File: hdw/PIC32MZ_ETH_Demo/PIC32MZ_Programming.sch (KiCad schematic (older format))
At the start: 10 parts

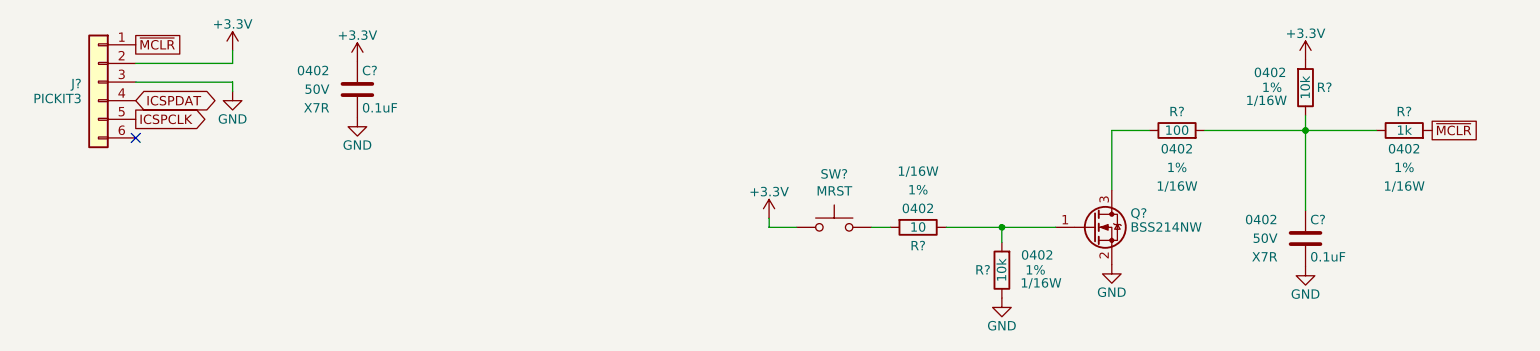
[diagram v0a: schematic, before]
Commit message: More schematic tweaks, followed PHY design guide
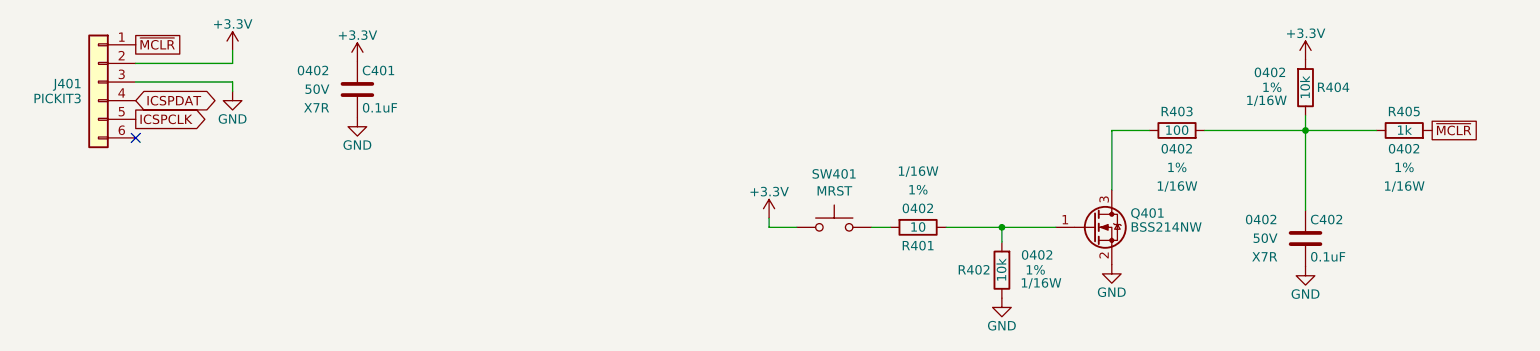
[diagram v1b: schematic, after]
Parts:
- gave numbers to parts that had none: 10
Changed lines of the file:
@@
 EESchema Schematic File Version 4
+LIBS:PIC32MZ_ETH_Demo-cache
 EELAYER 30 0
 EELAYER END
@@
 $EndDescr
 $Comp
-L Connector_Generic:Conn_01x06 J?
+L Connector_Generic:Conn_01x06 J401
 U 1 1 5BB4A695
 P 1070 1990
-F 0 "J?" H 1160 1980 50  0000 L CNN
+F 0 "J401" H 1160 1980 50  0000 L CNN
 F 1 "PICKIT3" H 1160 1900 50  0000 L CNN
 F 2 "Custom Footprints Library:PICKIT3_Header" H 1070 1990 50  0001 C CNN
@@
 ICSPCLK
 $Comp
-L power:GND #PWR?
+L power:GND #PWR0402
 U 1 1 5BB4A7C4
 P 1790 2040
-F 0 "#PWR?" H 1790 1790 50  0001 C CNN
+F 0 "#PWR0402" H 1790 1790 50  0001 C CNN
 F 1 "GND" H 1790 1890 50  0000 C CNN
 F 2 "" H 1790 2040 50  0001 C CNN
@@
 NoConn ~ 1270 2290
 $Comp
-L Custom_Library:C_Custom C?
+L Custom_Library:C_Custom C401
 U 1 1 5BC13497
 P 2460 2030
-F 0 "C?" H 2485 2130 50  0000 L CNN
+F 0 "C401" H 2485 2130 50  0000 L CNN
 F 1 "0.1uF" H 2485 1930 50  0000 L CNN
 F 2 "Capacitors_SMD:C_0402" H 2498 1880 50  0001 C CNN
@@
 $EndComp
 $Comp
-L power:GND #PWR?
+L power:GND #PWR0404
 U 1 1 5BC1349E
 P 2460 2180
-F 0 "#PWR?" H 2460 1930 50  0001 C CNN
+F 0 "#PWR0404" H 2460 1930 50  0001 C CNN
 F 1 "GND" H 2460 2030 50  0000 C CNN
 F 2 "" H 2460 2180 50  0001 C CNN
@@
 AR Path="/5C1D5CB6/5BC152E5" Ref="R?"  Part="1"
 AR Path="/5CB0BC26/5BC152E5" Ref="R?"  Part="1"
-AR Path="/5E697920/5BC152E5" Ref="R?"  Part="1"
-F 0 "R?" H 7490 2020 50  0000 R CNN
+AR Path="/5E697920/5BC152E5" Ref="R404"  Part="1"
+F 0 "R404" H 7490 2020 50  0000 R CNN
 F 1 "10k" V 7550 2020 50  0000 C CNN
 F 2 "Resistors_SMD:R_0402" H 7550 2020 50  0001 C CNN
@@
 $EndComp
 $Comp
-L Custom_Library:C_Custom C?
+L Custom_Library:C_Custom C402
 U 1 1 5BC1574E
 P 7550 2830
-F 0 "C?" H 7575 2930 50  0000 L CNN
+F 0 "C402" H 7575 2930 50  0000 L CNN
 F 1 "0.1uF" H 7575 2730 50  0000 L CNN
 F 2 "Capacitors_SMD:C_0402" H 7588 2680 50  0001 C CNN
@@
 $EndComp
 $Comp
-L power:GND #PWR?
+L power:GND #PWR0409
 U 1 1 5BC15E18
 P 7550 2980
-F 0 "#PWR?" H 7550 2730 50  0001 C CNN
+F 0 "#PWR0409" H 7550 2730 50  0001 C CNN
 F 1 "GND" H 7550 2830 50  0000 C CNN
 F 2 "" H 7550 2980 50  0001 C CNN
@@
 $EndComp
 $Comp
-L Custom_Library:R_Custom R?
+L Custom_Library:R_Custom R405
 U 1 1 5BC16316
 P 8080 2250
-F 0 "R?" V 7980 2250 50  0000 C CNN
+F 0 "R405" V 7980 2250 50  0000 C CNN
 F 1 "1k" V 8080 2250 50  0000 C CNN
 F 2 "Resistors_SMD:R_0402" H 8080 2250 50  0001 C CNN
@@
 ~MCLR
 $Comp
-L Switch:SW_Push SW?
+L Switch:SW_Push SW401
 U 1 1 5BC17B44
 P 5020 2770
-F 0 "SW?" H 5020 3055 50  0000 C CNN
+F 0 "SW401" H 5020 3055 50  0000 C CNN
 F 1 "MRST" H 5020 2964 50  0000 C CNN
 F 2 "Buttons_Switches_THT:SW_PUSH_6mm" H 5020 2970 50  0001 C CNN
@@
 $EndComp
 $Comp
-L Custom_Library:R_Custom R?
+L Custom_Library:R_Custom R403
 U 1 1 5BC190FF
 P 6860 2250
-F 0 "R?" V 6760 2250 50  0000 C CNN
+F 0 "R403" V 6760 2250 50  0000 C CNN
 F 1 "100" V 6860 2250 50  0000 C CNN
 F 2 "Resistors_SMD:R_0402" H 6860 2250 50  0001 C CNN
@@
 	7010 2250 7550 2250
 $Comp
-L power:GND #PWR?
+L power:GND #PWR0407
 U 1 1 5BE087C1
 P 6510 2970
-F 0 "#PWR?" H 6510 2720 50  0001 C CNN
+F 0 "#PWR0407" H 6510 2720 50  0001 C CNN
 F 1 "GND" H 6510 2820 50  0000 C CNN
 F 2 "" H 6510 2970 50  0001 C CNN
@@
 $EndComp
 $Comp
-L Custom_Library:R_Custom R?
+L Custom_Library:R_Custom R401
 U 1 1 5BE087CB
 P 5470 2770
-F 0 "R?" V 5370 2770 50  0000 C CNN
+F 0 "R401" V 5370 2770 50  0000 C CNN
 F 1 "10" V 5470 2770 50  0000 C CNN
 F 2 "Resistors_SMD:R_0402" H 5470 2770 50  0001 C CNN
@@
 AR Path="/5C1D5CB6/5BE087D6" Ref="R?"  Part="1"
 AR Path="/5CB0BC26/5BE087D6" Ref="R?"  Part="1"
-AR Path="/5E697920/5BE087D6" Ref="R?"  Part="1"
-F 0 "R?" H 5860 3000 50  0000 R CNN
+AR Path="/5E697920/5BE087D6" Ref="R402"  Part="1"
+F 0 "R402" H 5860 3000 50  0000 R CNN
 F 1 "10k" V 5920 3000 50  0000 C CNN
 F 2 "Resistors_SMD:R_0402" H 5920 3000 50  0001 C CNN
@@
 $EndComp
 $Comp
-L power:GND #PWR?
+L power:GND #PWR0406
 U 1 1 5BE087DD
 P 5920 3150
-F 0 "#PWR?" H 5920 2900 50  0001 C CNN
+F 0 "#PWR0406" H 5920 2900 50  0001 C CNN
 F 1 "GND" H 5920 3000 50  0000 C CNN
 F 2 "" H 5920 3150 50  0001 C CNN
@@
 	7550 2680 7550 2250
 $Comp
-L power:+3.3V #PWR?
+L power:+3.3V #PWR0405
 U 1 1 5E6EB62A
 P 4670 2720
-F 0 "#PWR?" H 4670 2570 50  0001 C CNN
+F 0 "#PWR0405" H 4670 2570 50  0001 C CNN
 F 1 "+3.3V" H 4670 2860 50  0000 C CNN
 F 2 "" H 4670 2720 50  0001 C CNN
@@
 $EndComp
 $Comp
-L power:+3.3V #PWR?
+L power:+3.3V #PWR0408
 U 1 1 5E6EBFA5
 P 7550 1870
-F 0 "#PWR?" H 7550 1720 50  0001 C CNN
+F 0 "#PWR0408" H 7550 1720 50  0001 C CNN
 F 1 "+3.3V" H 7550 2010 50  0000 C CNN
 F 2 "" H 7550 1870 50  0001 C CNN
@@
 $EndComp
 $Comp
-L power:+3.3V #PWR?
+L power:+3.3V #PWR0403
 U 1 1 5E6EC62F
 P 2460 1880
-F 0 "#PWR?" H 2460 1730 50  0001 C CNN
+F 0 "#PWR0403" H 2460 1730 50  0001 C CNN
 F 1 "+3.3V" H 2460 2020 50  0000 C CNN
 F 2 "" H 2460 1880 50  0001 C CNN
@@
 $EndComp
 $Comp
-L power:+3.3V #PWR?
+L power:+3.3V #PWR0401
 U 1 1 5E6ECA36
 P 1790 1820
-F 0 "#PWR?" H 1790 1670 50  0001 C CNN
+F 0 "#PWR0401" H 1790 1670 50  0001 C CNN
 F 1 "+3.3V" H 1790 1960 50  0000 C CNN
 F 2 "" H 1790 1820 50  0001 C CNN
@@
 $EndComp
 $Comp
-L Transistor_FET:BSS214NW Q?
+L Transistor_FET:BSS214NW Q401
 U 1 1 5E765004
 P 6410 2770
-F 0 "Q?" H 6610 2845 50  0000 L CNN
+F 0 "Q401" H 6610 2845 50  0000 L CNN
 F 1 "BSS214NW" H 6610 2770 50  0000 L CNN
 F 2 "Package_TO_SOT_SMD:SOT-323_SC-70" H 6610 2695 50  0001 L CIN

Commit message: Populated digi-key pn's
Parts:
- C401, C402: Digi-Key PN (none) -> 490-10701-1-ND
- R401: Digi-Key PN (none) -> 541-3964-1-ND
- R402, R404: Digi-Key PN (none) -> RMCF0402FT10K0CT-ND
- R403: Digi-Key PN (none) -> 541-100LCT-ND
- R405: Digi-Key PN (none) -> 541-1.00KLCT-ND
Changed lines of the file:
@@
 F 5 "50V" H 2310 2030 50  0000 R CNN "Voltage"
 F 6 "X7R" H 2310 1930 50  0000 R CNN "Dielectric"
-F 7 "" H 2885 2530 60  0001 C CNN "Digi-Key PN"
+F 7 "490-10701-1-ND" H 2885 2530 60  0001 C CNN "Digi-Key PN"
 	1    2460 2030
 	1    0    0    -1
@@
 F 5 "1%" H 7730 2020 50  0000 C CNN "Tolerance"
 F 6 "1/16W" H 7760 1950 50  0000 C CNN "Wattage"
-F 7 "" H 7850 2420 60  0001 C CNN "Digi-Key PN"
+F 7 "RMCF0402FT10K0CT-ND" H 7850 2420 60  0001 C CNN "Digi-Key PN"
 	1    7550 2020
 	-1   0    0    -1
@@
 F 5 "50V" H 7400 2830 50  0000 R CNN "Voltage"
 F 6 "X7R" H 7400 2730 50  0000 R CNN "Dielectric"
-F 7 "" H 7975 3330 60  0001 C CNN "Digi-Key PN"
+F 7 "490-10701-1-ND" H 7975 3330 60  0001 C CNN "Digi-Key PN"
 	1    7550 2830
 	1    0    0    -1
@@
 F 5 "1%" V 8280 2250 50  0000 C CNN "Tolerance"
 F 6 "1/16W" V 8380 2250 50  0000 C CNN "Wattage"
-F 7 "" H 8380 2650 60  0001 C CNN "Digi-Key PN"
+F 7 "541-1.00KLCT-ND" H 8380 2650 60  0001 C CNN "Digi-Key PN"
 	1    8080 2250
 	0    1    1    0
@@
 F 5 "1%" V 7060 2250 50  0000 C CNN "Tolerance"
 F 6 "1/16W" V 7160 2250 50  0000 C CNN "Wattage"
-F 7 "" H 7160 2650 60  0001 C CNN "Digi-Key PN"
+F 7 "541-100LCT-ND" H 7160 2650 60  0001 C CNN "Digi-Key PN"
 	1    6860 2250
 	0    1    1    0
@@
 F 5 "1%" V 5670 2770 50  0000 C CNN "Tolerance"
 F 6 "1/16W" V 5770 2770 50  0000 C CNN "Wattage"
-F 7 "" H 5770 3170 60  0001 C CNN "Digi-Key PN"
+F 7 "541-3964-1-ND" H 5770 3170 60  0001 C CNN "Digi-Key PN"
 	1    5470 2770
 	0    -1   -1   0
@@
 F 5 "1%" H 6100 3000 50  0000 C CNN "Tolerance"
 F 6 "1/16W" H 6130 2930 50  0000 C CNN "Wattage"
-F 7 "" H 6220 3400 60  0001 C CNN "Digi-Key PN"
+F 7 "RMCF0402FT10K0CT-ND" H 6220 3400 60  0001 C CNN "Digi-Key PN"
 	1    5920 3000
 	1    0    0    -1
